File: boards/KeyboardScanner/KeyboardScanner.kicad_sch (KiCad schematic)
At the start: 14 parts, among them J1 Keyboard1, J2 Keyboard1, J3 Encoder, U5 ULN2803A, U8 4069

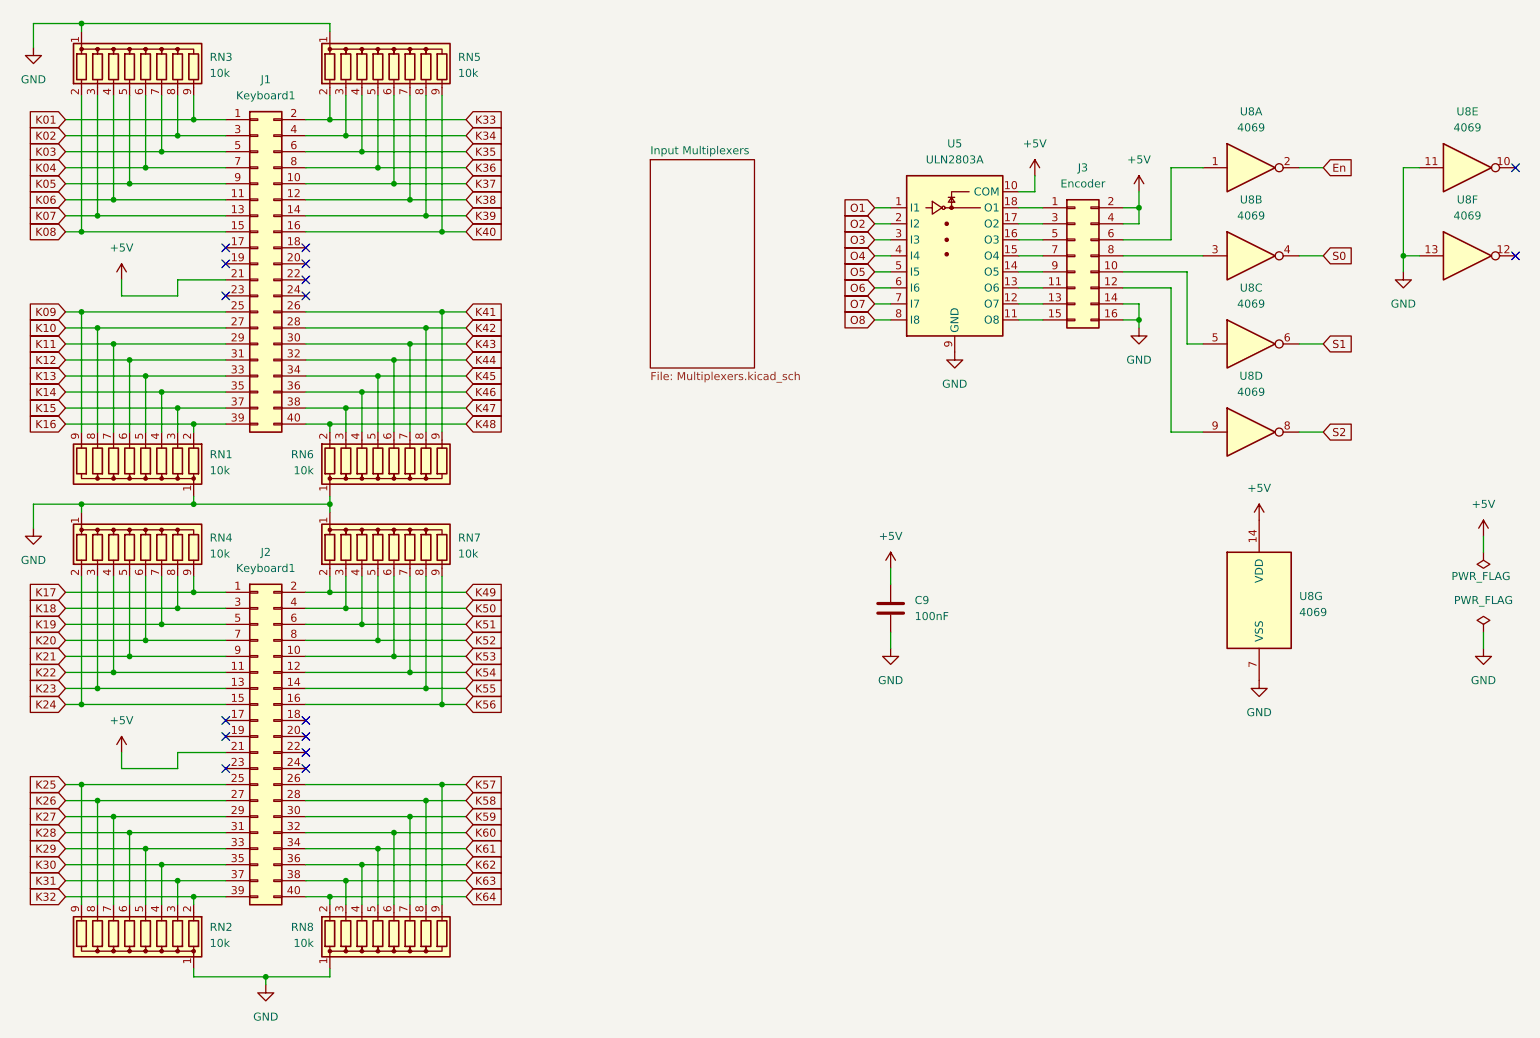
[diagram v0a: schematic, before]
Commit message: PCB layout for keyboard scanner and piston encoder
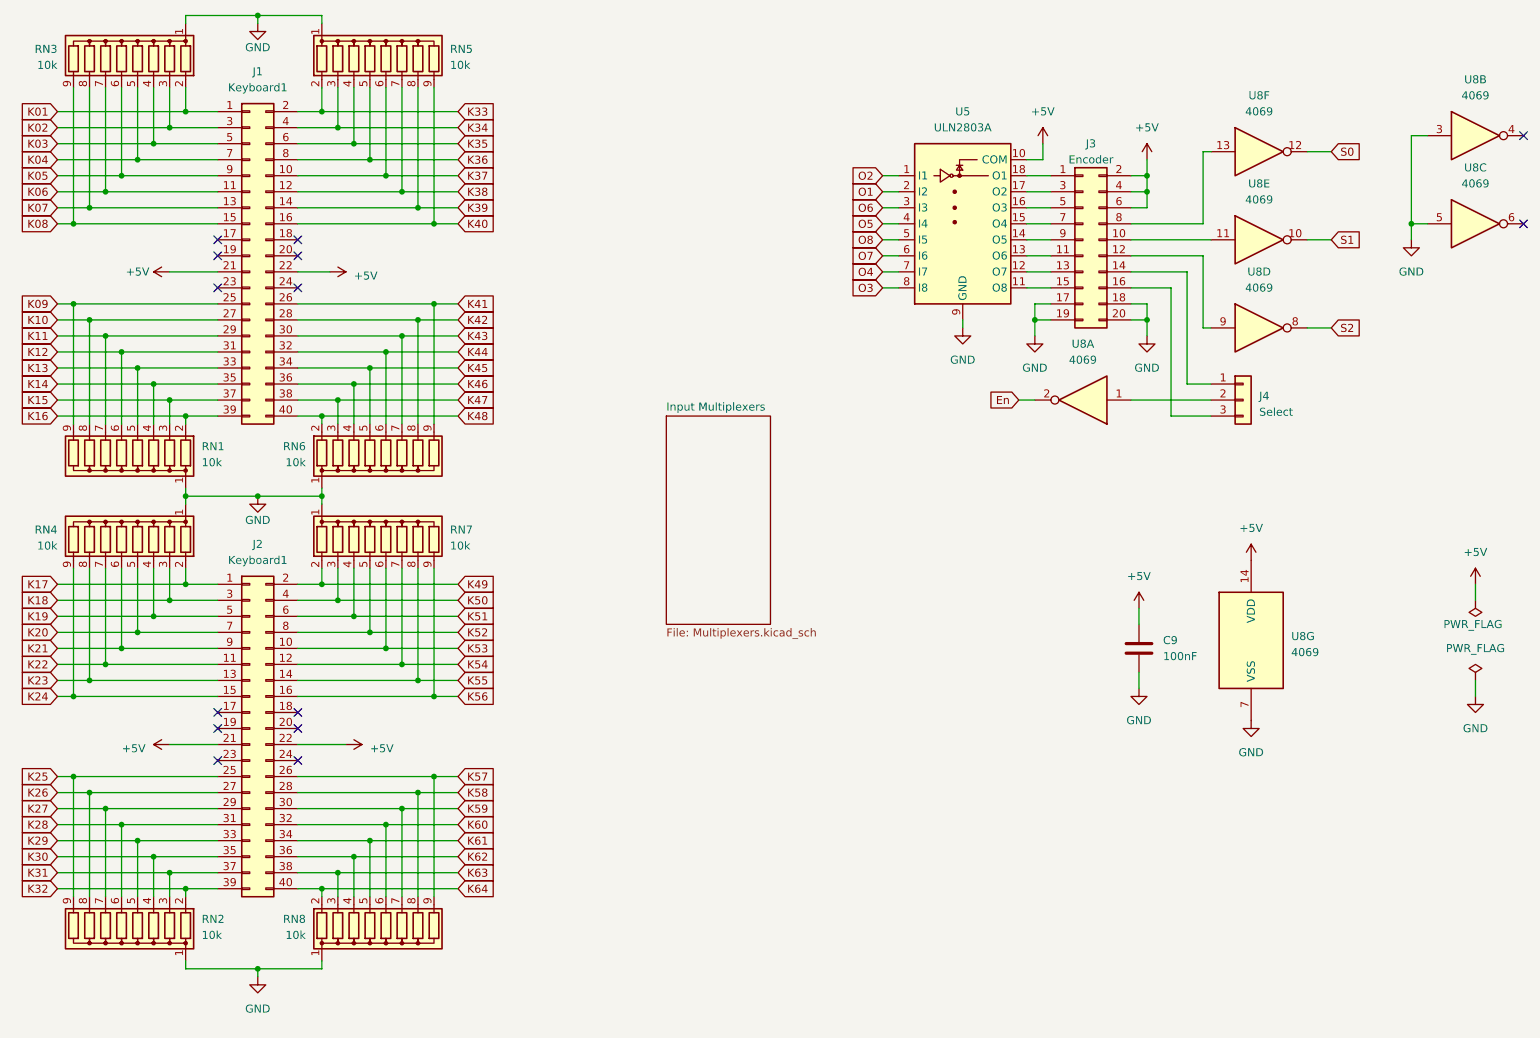
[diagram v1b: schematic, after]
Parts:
- removed J3: Encoder, Connector_IDC:IDC-Header_2x08_P2.54mm_Vertical, symbol Connector_Generic:Conn_02x08_Odd_Even
- added J3: Encoder, Connector_IDC:IDC-Header_2x10_P2.54mm_Horizontal, symbol Connector_Generic:Conn_02x10_Odd_Even
- added J4: Select, Connector_PinHeader_2.54mm:PinHeader_1x03_P2.54mm_Vertical, symbol Connector_Generic:Conn_01x03
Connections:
- net +5V: now also J1.22 (Pin_22), J2.22 (Pin_22), J3.2 (Pin_2), J3.4 (Pin_4), J3.6 (Pin_6)
- net GND: now also U8.3, U8.5, J3.17 (Pin_17), J3.18 (Pin_18), J3.19 (Pin_19), J3.20 (Pin_20); no longer U8.11, U8.13
- net K01: now also RN3.2 (R1); no longer RN3.9 (R8)
- net K02: now also RN3.3 (R2); no longer RN3.8 (R7)
- net K03: now also RN3.4 (R3); no longer RN3.7 (R6)
- net K04: now also RN3.5 (R4); no longer RN3.6 (R5)
- net K05: now also RN3.6 (R5); no longer RN3.5 (R4)
- net K06: now also RN3.7 (R6); no longer RN3.4 (R3)
- net K07: now also RN3.8 (R7); no longer RN3.3 (R2)
- net K08: now also RN3.9 (R8); no longer RN3.2 (R1)
- net K17: now also RN4.2 (R1); no longer RN4.9 (R8)
- net K18: now also RN4.3 (R2); no longer RN4.8 (R7)
- net K19: now also RN4.4 (R3); no longer RN4.7 (R6)
- net K20: now also RN4.5 (R4); no longer RN4.6 (R5)
- net K21: now also RN4.6 (R5); no longer RN4.5 (R4)
- net K22: now also RN4.7 (R6); no longer RN4.4 (R3)
- net K23: now also RN4.8 (R7); no longer RN4.3 (R2)
- net K24: now also RN4.9 (R8); no longer RN4.2 (R1)
- net O1: now also U5.2 (I2); no longer U5.1 (I1)
- net O2: now also U5.1 (I1); no longer U5.2 (I2)
- net O3: now also U5.8 (I8); no longer U5.3 (I3)
- net O4: now also U5.7 (I7); no longer U5.4 (I4)
- net O5: now also U5.4 (I4); no longer U5.5 (I5)
- net O6: now also U5.3 (I3); no longer U5.6 (I6)
- net O7: now also U5.6 (I6); no longer U5.7 (I7)
- net O8: now also U5.5 (I5); no longer U5.8 (I8)
- net S0: now also U8.12; no longer U8.4
- net S1: now also U8.10; no longer U8.6
- net at U5.11 (O8): now also J3.15 (Pin_15)
- net at U5.12 (O7): now also J3.13 (Pin_13)
- net at U5.13 (O6): now also J3.11 (Pin_11)
- net at U5.14 (O5): now also J3.9 (Pin_9)
- net at U5.15 (O4): now also J3.7 (Pin_7)
- net at U5.16 (O3): now also J3.5 (Pin_5)
- net at U5.17 (O2): now also J3.3 (Pin_3)
- net at U5.18 (O1): now also J3.1 (Pin_1)
- net at U8.9: now also J3.12 (Pin_12)
- net at U8.1: now also J4.2 (Pin_2)
- new net: J3.10 (Pin_10), U8.11
- new net: J3.14 (Pin_14), J4.1 (Pin_1)
- new net: J3.16 (Pin_16), J4.3 (Pin_3)
- new net: J3.8 (Pin_8), U8.13
- no-connect marks 16 -> 14
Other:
- moved on the sheet: C9, U8G

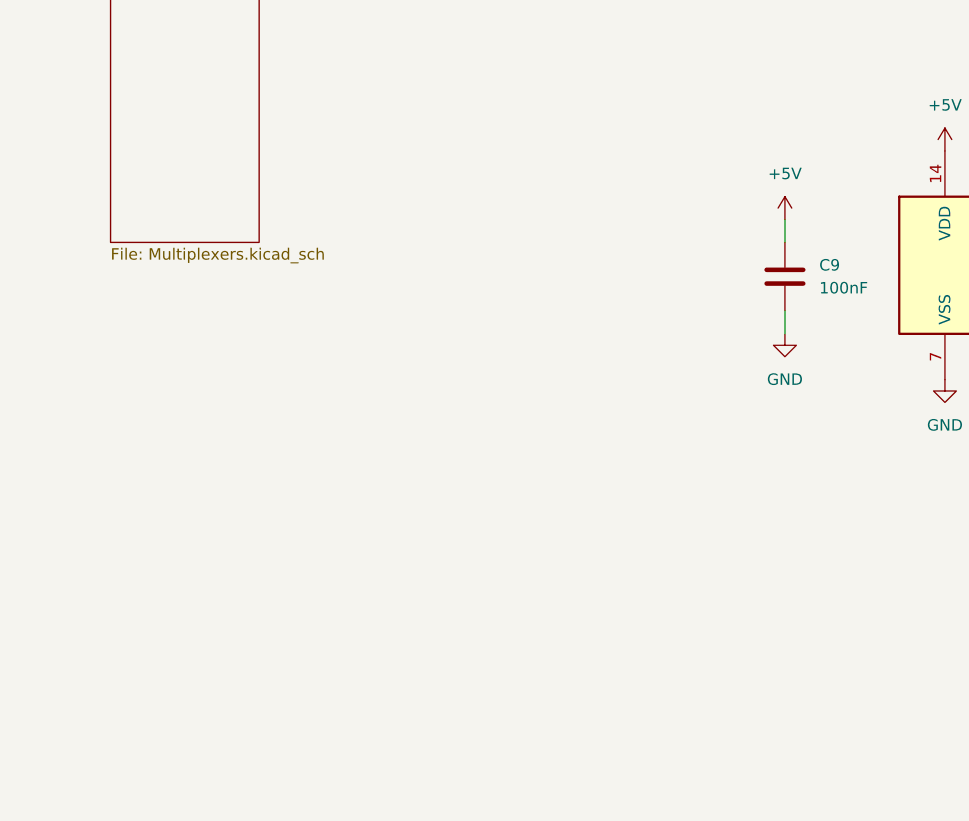
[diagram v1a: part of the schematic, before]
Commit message: Updated to KiCAD 8, fixed optocouplers for MIDI and added powersupplies
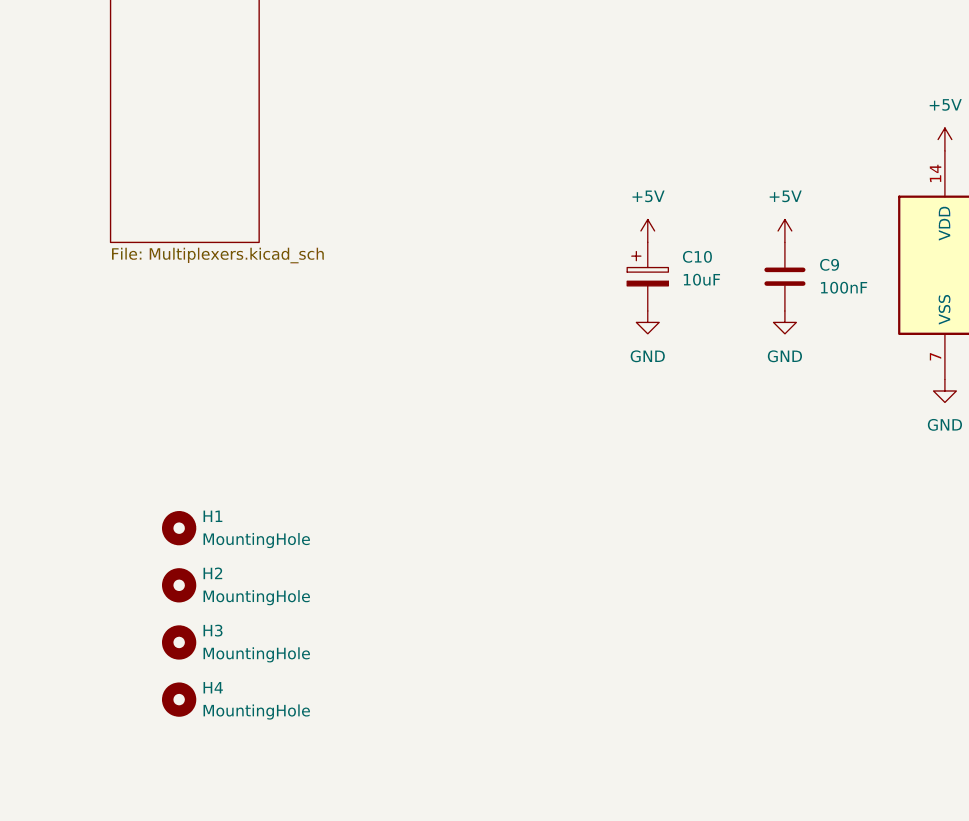
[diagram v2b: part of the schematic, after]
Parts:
- added C10: 10uF, Capacitor_THT:CP_Radial_D6.3mm_P2.50mm, symbol Device:C_Polarized
- added H1, H2, H3, H4: MountingHole, MountingHole:MountingHole_3.2mm_M3, symbol Mechanical:MountingHole
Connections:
- net +5V: now also C10.1
- net GND: now also C10.2

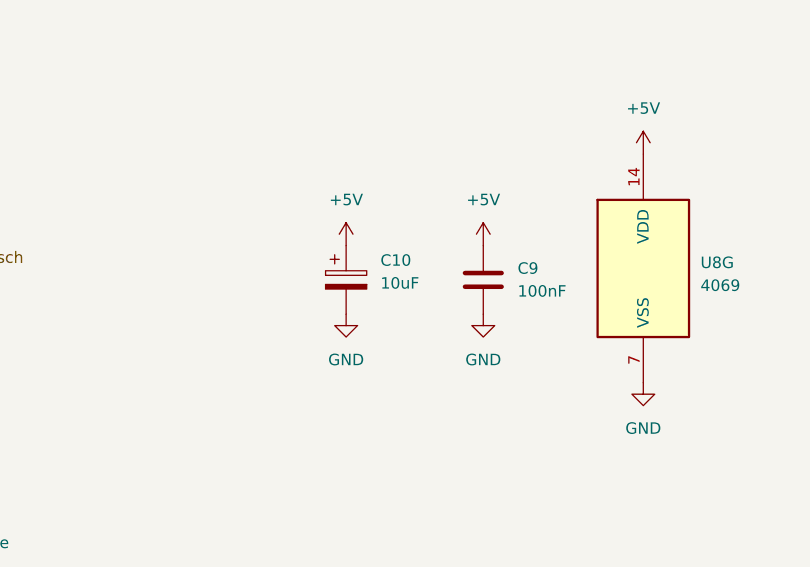
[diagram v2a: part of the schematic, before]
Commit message: Updated design rules to 0.32mm template and exported Gerber files
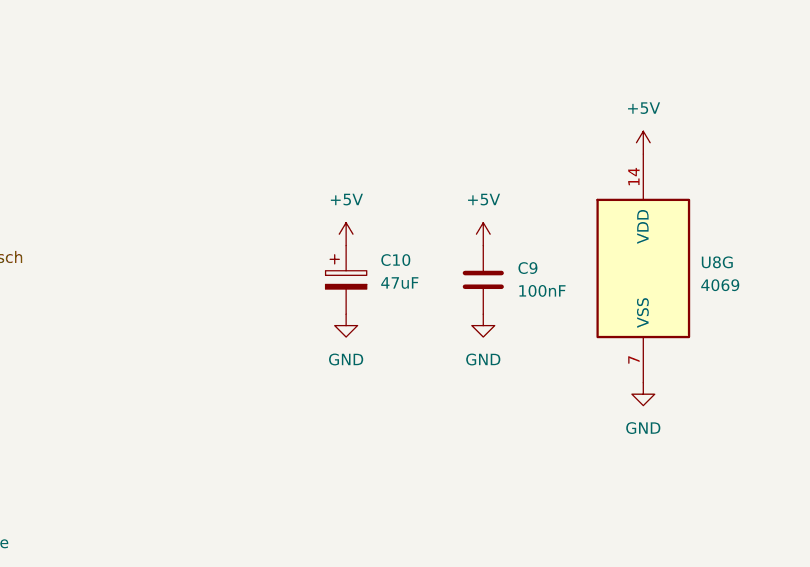
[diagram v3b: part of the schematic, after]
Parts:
- C10: value 10uF -> 47uF
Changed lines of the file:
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@@
 			)
 		)
-		(property "Value" "10uF"
+		(property "Value" "47uF"
 			(at 198.12 126.1109 0)
 			(effects

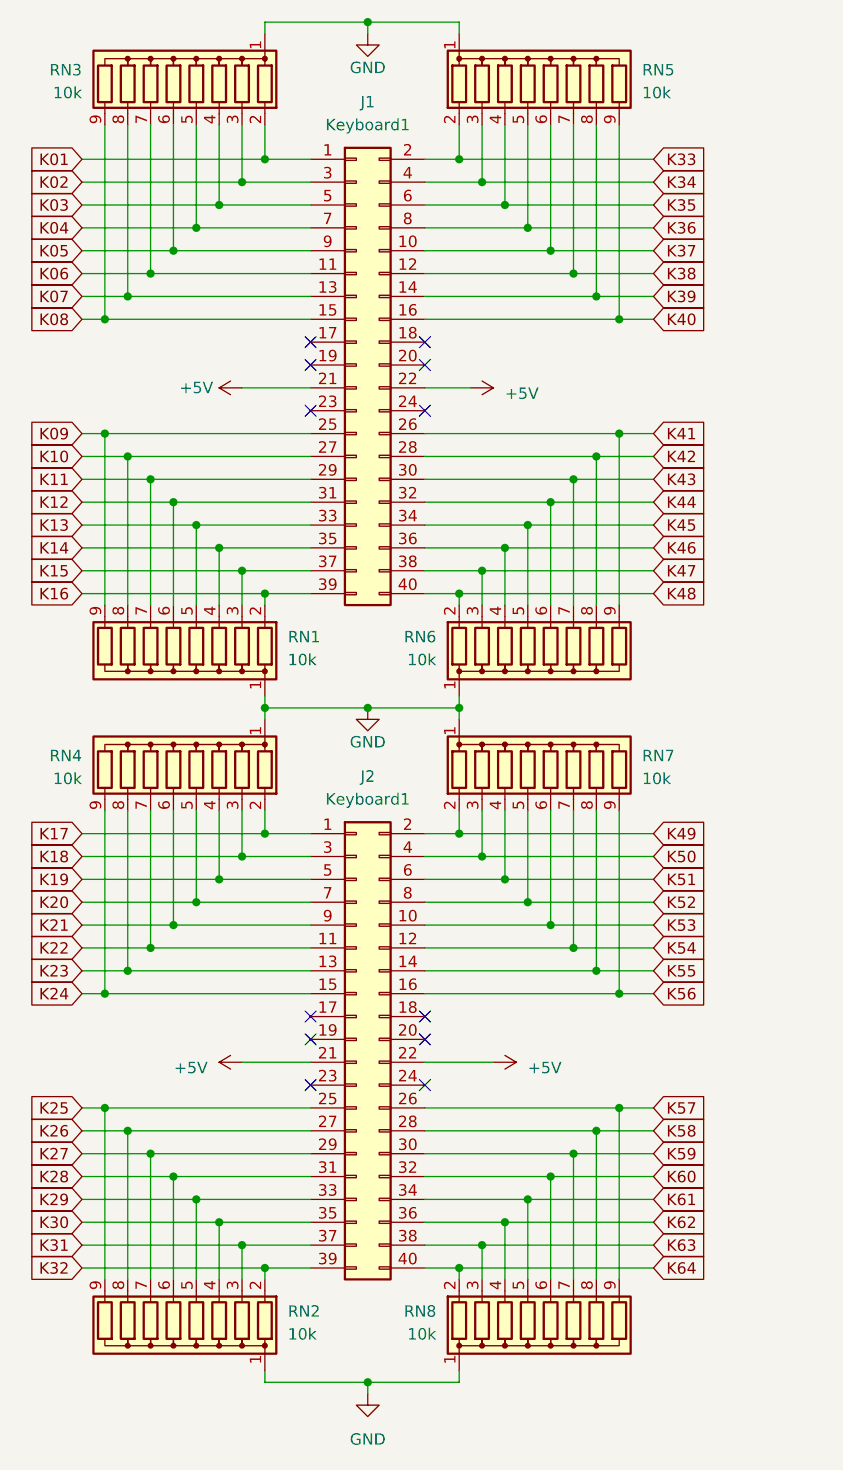
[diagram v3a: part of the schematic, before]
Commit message: Fixed pulldown resistors for KeyboardScanner
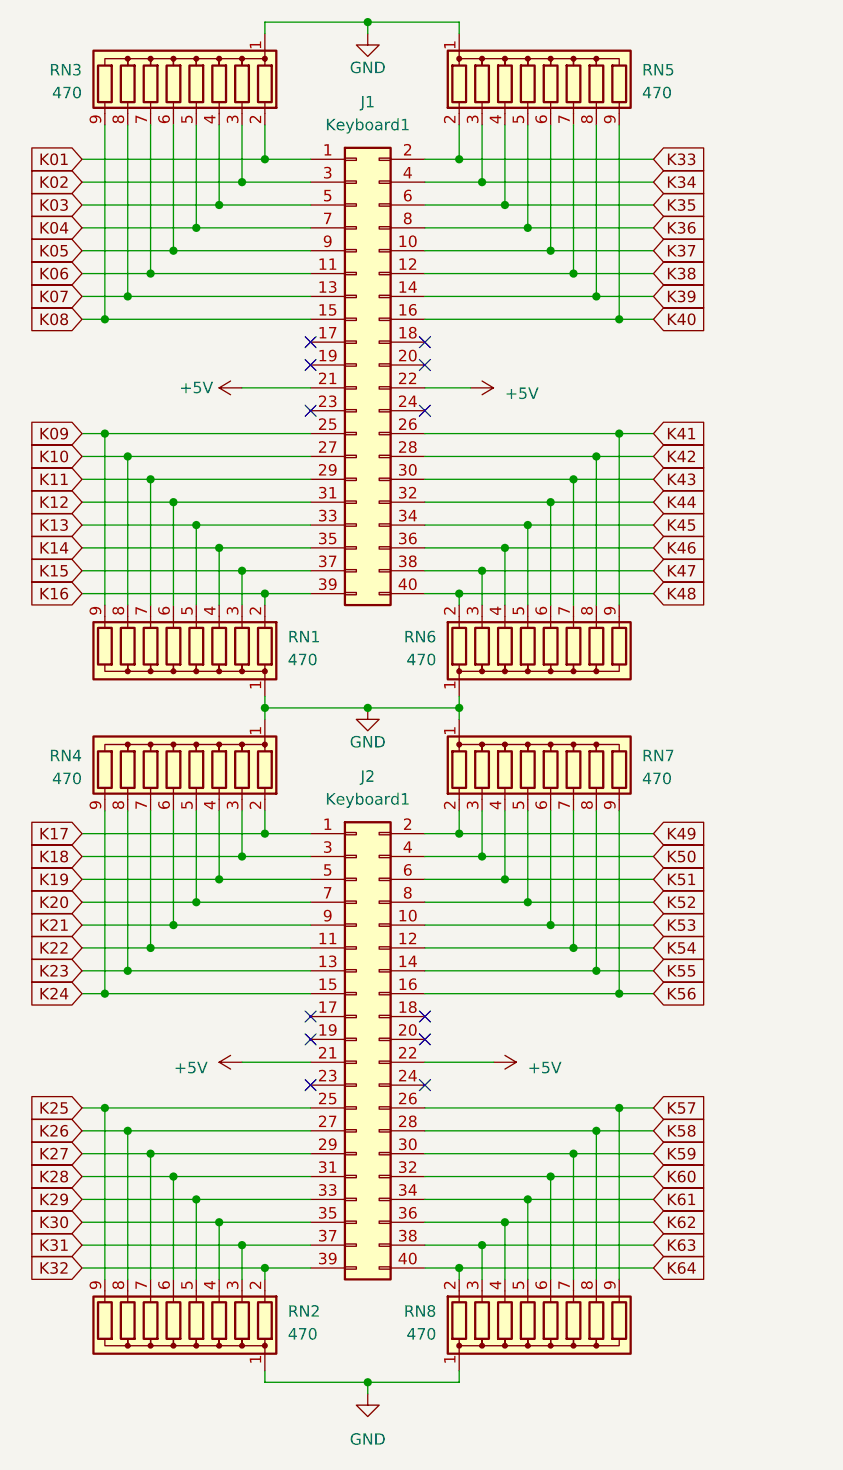
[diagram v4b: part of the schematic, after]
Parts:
- RN1, RN2, RN3, RN4, RN5, RN6, RN7, RN8: value 10k -> 470
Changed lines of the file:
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@@
 			)
 		)
-		(property "Value" "10k"
+		(property "Value" "470"
 			(at 60.96 96.2659 0)
 			(effects
@@
 			)
 		)
-		(property "Value" "10k"
+		(property "Value" "470"
 			(at 77.47 96.2659 0)
 			(effects
@@
 			)
 		)
-		(property "Value" "10k"
+		(property "Value" "470"
 			(at 60.96 171.1959 0)
 			(effects
@@
 			)
 		)
-		(property "Value" "10k"
+		(property "Value" "470"
 			(at 38.1 109.4739 0)
 			(effects
@@
 			)
 		)
-		(property "Value" "10k"
+		(property "Value" "470"
 			(at 100.33 109.4739 0)
 			(effects
@@
 			)
 		)
-		(property "Value" "10k"
+		(property "Value" "470"
 			(at 38.1 33.2739 0)
 			(effects
@@
 			)
 		)
-		(property "Value" "10k"
+		(property "Value" "470"
 			(at 100.33 33.2739 0)
 			(effects
@@
 			)
 		)
-		(property "Value" "10k"
+		(property "Value" "470"
 			(at 77.47 171.1959 0)
 			(effects
